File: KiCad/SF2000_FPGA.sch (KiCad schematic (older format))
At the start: 15 parts, among them J10 Conn_02x01, J3 Conn_02x03_Odd_Even, J4 Conn_02x01, J8 Conn_02x01, J9 Conn_02x01, U18 74LVC2G14, U7 10M04SCE144

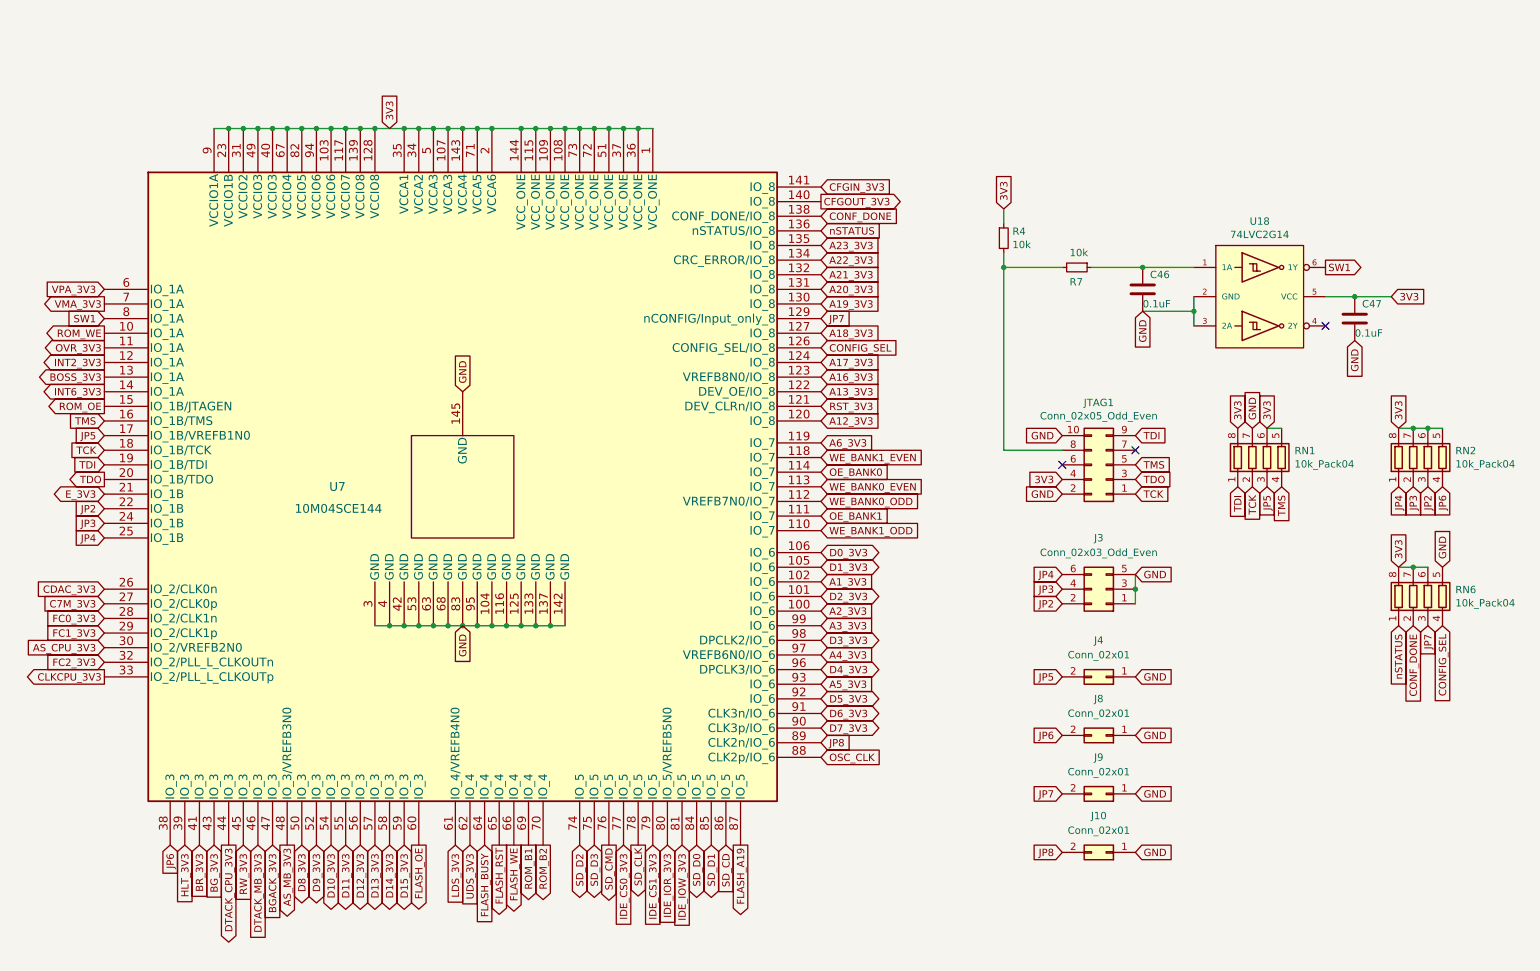
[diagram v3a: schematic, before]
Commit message: added IDE Activity LED-header and a header for IDE-pin 39 /Active
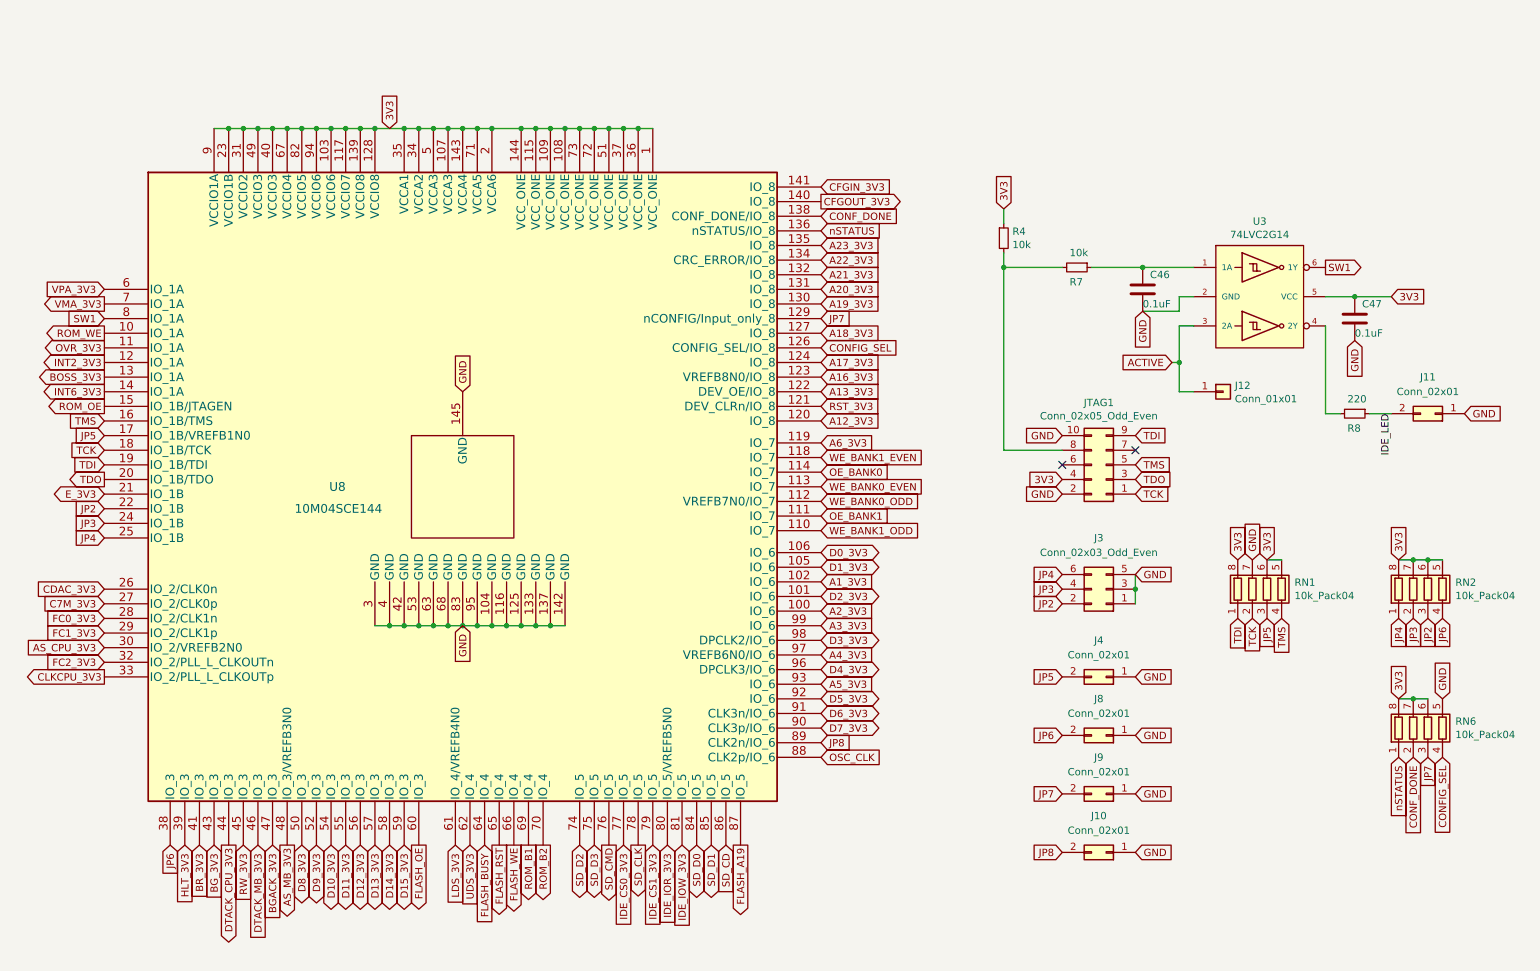
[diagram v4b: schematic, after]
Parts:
- added J11: Conn_02x01, Connector_PinHeader_2.54mm:PinHeader_2x01_P2.54mm_Vertical, symbol Connector_Generic:Conn_02x01
- added J12: Conn_01x01, Connector_PinHeader_2.54mm:PinHeader_1x01_P2.54mm_Vertical, symbol Connector_Generic:Conn_01x01
- added R8: 220, Resistor_SMD:R_0805_2012Metric_Pad1.15x1.40mm_HandSolder, symbol Device:R_Small
- renumbered U18 to U3
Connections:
- net GND: now also J11.1 (Pin_1); no longer U3.3 (2A)
- net at U3.4 (2Y): now also R8.2
- new net ACTIVE: J12.1 (Pin_1), U3.3 (2A)
- new net IDE_LED: J11.2 (Pin_2), R8.1
- no-connect marks 3 -> 2
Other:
- moved on the sheet: RN1, RN2, RN6
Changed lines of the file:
@@
 P 3800 3550
 AR Path="/62146C83" Ref="U7"  Part="1"
-AR Path="/620D263D/62146C83" Ref="U7"  Part="1"
-F 0 "U7" H 3000 3550 60  0000 R CNN
+AR Path="/620D263D/62146C83" Ref="U8"  Part="1"
+F 0 "U8" H 3000 3550 60  0000 R CNN
 F 1 "10M04SCE144" H 3250 3400 60  0000 R CNN
 F 2 "SF2000:EQFP-144-1EP_20x20mm_P0.5mm_EP5x5mm_TH_GND_pad" H 3800 3900 60  0001 C CNN
@@
 L Device:R_Pack04 RN1
 U 1 1 625F56E7
-P 9300 3350
-F 0 "RN1" H 9488 3396 50  0000 L CNN
-F 1 "10k_Pack04" H 9488 3305 50  0000 L CNN
-F 2 "SF2000:RESCAF80P320X160X60-8N" V 9575 3350 50  0001 C CNN
-F 3 "~" H 9300 3350 50  0001 C CNN
-	1    9300 3350
-	1    0    0    -1
-$EndComp
-Text GLabel 9100 3150 1    50   Input ~ 0
-3V3
-Text GLabel 9100 3550 3    50   Input ~ 0
+P 9300 4250
+F 0 "RN1" H 9488 4296 50  0000 L CNN
+F 1 "10k_Pack04" H 9488 4205 50  0000 L CNN
+F 2 "SF2000:RESCAF80P320X160X60-8N" V 9575 4250 50  0001 C CNN
+F 3 "~" H 9300 4250 50  0001 C CNN
+	1    9300 4250
+	1    0    0    -1
+$EndComp
+Text GLabel 9100 4050 1    50   Input ~ 0
+3V3
+Text GLabel 9100 4450 3    50   Input ~ 0
 TDI
-Text GLabel 9200 3550 3    50   Input ~ 0
+Text GLabel 9200 4450 3    50   Input ~ 0
 TCK
-Text GLabel 9400 3550 3    50   Input ~ 0
+Text GLabel 9400 4450 3    50   Input ~ 0
 TMS
-Text GLabel 9300 3550 3    50   Input ~ 0
+Text GLabel 9300 4450 3    50   Input ~ 0
 JP5
-Text GLabel 9200 3150 1    50   Input ~ 0
+Text GLabel 9200 4050 1    50   Input ~ 0
 GND
 Text GLabel 1350 3700 0    50   Input ~ 0
 JP2
-Text GLabel 9300 3150 1    50   Input ~ 0
-3V3
-Wire Wire Line
-	9300 3150 9400 3150
+Text GLabel 9300 4050 1    50   Input ~ 0
+3V3
+Wire Wire Line
+	9300 4050 9400 4050
 $Comp
 L Device:R_Pack04 RN2
 U 1 1 6265DCDE
-P 10400 3350
-F 0 "RN2" H 10588 3396 50  0000 L CNN
-F 1 "10k_Pack04" H 10588 3305 50  0000 L CNN
-F 2 "SF2000:RESCAF80P320X160X60-8N" V 10675 3350 50  0001 C CNN
-F 3 "~" H 10400 3350 50  0001 C CNN
-	1    10400 3350
-	1    0    0    -1
-$EndComp
-Text GLabel 10200 3150 1    50   Input ~ 0
-3V3
-Wire Wire Line
-	10200 3150 10300 3150
-Connection ~ 10300 3150
-Wire Wire Line
-	10300 3150 10400 3150
-Connection ~ 10400 3150
-Wire Wire Line
-	10400 3150 10500 3150
-Text GLabel 10200 4500 3    50   Input ~ 0
+P 10400 4250
+F 0 "RN2" H 10588 4296 50  0000 L CNN
+F 1 "10k_Pack04" H 10588 4205 50  0000 L CNN
+F 2 "SF2000:RESCAF80P320X160X60-8N" V 10675 4250 50  0001 C CNN
+F 3 "~" H 10400 4250 50  0001 C CNN
+	1    10400 4250
+	1    0    0    -1
+$EndComp
+Text GLabel 10200 4050 1    50   Input ~ 0
+3V3
+Wire Wire Line
+	10200 4050 10300 4050
+Connection ~ 10300 4050
+Wire Wire Line
+	10300 4050 10400 4050
+Connection ~ 10400 4050
+Wire Wire Line
+	10400 4050 10500 4050
+Text GLabel 10200 5400 3    50   Input ~ 0
 nSTATUS
-Text GLabel 10300 4500 3    50   Input ~ 0
+Text GLabel 10300 5400 3    50   Input ~ 0
 CONF_DONE
-Text GLabel 10200 3550 3    50   Input ~ 0
+Text GLabel 10200 4450 3    50   Input ~ 0
 JP4
-Text GLabel 10300 3550 3    50   Input ~ 0
+Text GLabel 10300 4450 3    50   Input ~ 0
 JP3
 Text GLabel 7500 1650 1    50   Input ~ 0
@@
 Text GLabel 1350 3200 0    50   Input ~ 0
 JP5
-Text GLabel 10400 3550 3    50   Input ~ 0
+Text GLabel 10400 4450 3    50   Input ~ 0
 JP2
 Text GLabel 1350 2300 0    50   Output ~ 0
@@
 L Device:R_Pack04 RN6
 U 1 1 62107318
-P 10400 4300
-F 0 "RN6" H 10588 4346 50  0000 L CNN
-F 1 "10k_Pack04" H 10588 4255 50  0000 L CNN
-F 2 "SF2000:RESCAF80P320X160X60-8N" V 10675 4300 50  0001 C CNN
-F 3 "~" H 10400 4300 50  0001 C CNN
-	1    10400 4300
-	1    0    0    -1
-$EndComp
-Text GLabel 10500 4500 3    50   Input ~ 0
+P 10400 5200
+F 0 "RN6" H 10588 5246 50  0000 L CNN
+F 1 "10k_Pack04" H 10588 5155 50  0000 L CNN
+F 2 "SF2000:RESCAF80P320X160X60-8N" V 10675 5200 50  0001 C CNN
+F 3 "~" H 10400 5200 50  0001 C CNN
+	1    10400 5200
+	1    0    0    -1
+$EndComp
+Text GLabel 10500 5400 3    50   Input ~ 0
 CONFIG_SEL
-Text GLabel 10200 4100 1    50   Input ~ 0
-3V3
-Wire Wire Line
-	10200 4100 10300 4100
-Text GLabel 10500 4100 1    50   Input ~ 0
+Text GLabel 10200 5000 1    50   Input ~ 0
+3V3
+Wire Wire Line
+	10200 5000 10300 5000
+Text GLabel 10500 5000 1    50   Input ~ 0
 GND
 Text GLabel 6250 2400 2    50   Input ~ 0
@@
 ROM_B2
 Wire Wire Line
-	10300 4100 10400 4100
-Connection ~ 10300 4100
-Text GLabel 10400 4500 3    50   Input ~ 0
+	10300 5000 10400 5000
+Connection ~ 10300 5000
+Text GLabel 10400 5400 3    50   Input ~ 0
 JP7
 Text GLabel 7900 5250 0    50   Input ~ 0
@@
 Text GLabel 8400 5250 2    50   Input ~ 0
 GND
-Text GLabel 10500 3550 3    50   Input ~ 0
+Text GLabel 10500 4450 3    50   Input ~ 0
 JP6
 Text GLabel 1800 6000 3    50   Input ~ 0
 JP6
 $Comp
-L SF2000:74LVC2G14 U18
+L SF2000:74LVC2G14 U3
 U 1 1 623FD973
 P 9250 2250
-F 0 "U18" H 9250 2765 50  0000 C CNN
+F 0 "U3" H 9250 2765 50  0000 C CNN
 F 1 "74LVC2G14" H 9250 2674 50  0000 C CNN
 F 2 "Package_SO:TSOP-6_1.65x3.05mm_P0.95mm" H 9750 3200 50  0001 C CNN
@@
 	1    0    0    -1
 $EndComp
-NoConn ~ 9700 2450
 Text GLabel 8450 2350 3    50   Input ~ 0
 GND
-Wire Wire Line
-	8800 2250 8800 2350
 Text GLabel 10150 2250 2    50   Input ~ 0
 3V3
 Wire Wire Line
 	8450 2050 8800 2050
-Wire Wire Line
-	8450 2350 8800 2350
-Connection ~ 8800 2350
-Wire Wire Line
-	8800 2350 8800 2450
 $Comp
 L Device:C C?
@@
 	8100 2050 8450 2050
 Connection ~ 8450 2050
+Wire Wire Line
+	8450 2350 8700 2350
+Wire Wire Line
+	8700 2350 8700 2250
+Wire Wire Line
+	8700 2250 8800 2250
+Text GLabel 8650 2700 0    50   Input ~ 0
+ACTIVE
+Wire Wire Line
+	8800 2450 8700 2450
+Wire Wire Line
+	8700 2450 8700 2700
+Wire Wire Line
+	8700 2700 8650 2700
+$Comp
+L Device:R_Small R?
+U 1 1 625C5BBC
+P 9900 3050
+AR Path="/625C5BBC" Ref="R?"  Part="1"
+AR Path="/620D263D/625C5BBC" Ref="R8"  Part="1"
+F 0 "R8" V 10000 3000 50  0000 L CNN
+F 1 "220" V 9800 3000 50  0000 L CNN
+F 2 "Resistor_SMD:R_0805_2012Metric_Pad1.15x1.40mm_HandSolder" H 9900 3050 50  0001 C CNN
+F 3 "~" H 9900 3050 50  0001 C CNN
+	1    9900 3050
+	0    1    1    0
+$EndComp
+Wire Wire Line
+	9700 2450 9700 3050
+Wire Wire Line
+	9700 3050 9800 3050
+$Comp
+L Connector_Generic:Conn_02x01 J11
+U 1 1 625CA23F
+P 10450 3050
+F 0 "J11" H 10500 2800 50  0000 C CNN
+F 1 "Conn_02x01" H 10500 2900 50  0000 C CNN
+F 2 "Connector_PinHeader_2.54mm:PinHeader_2x01_P2.54mm_Vertical" H 10450 3050 50  0001 C CNN
+F 3 "~" H 10450 3050 50  0001 C CNN
+	1    10450 3050
+	-1   0    0    1
+$EndComp
+Wire Wire Line
+	10000 3050 10150 3050
+Text GLabel 10650 3050 2    50   Input ~ 0
+GND
+Text Label 10150 3050 3    50   ~ 0
+IDE_LED
+$Comp
+L Connector_Generic:Conn_01x01 J12
+U 1 1 62602244
+P 9000 2900
+F 0 "J12" H 9080 2942 50  0000 L CNN
+F 1 "Conn_01x01" H 9080 2851 50  0000 L CNN
+F 2 "Connector_PinHeader_2.54mm:PinHeader_1x01_P2.54mm_Vertical" H 9000 2900 50  0001 C CNN
+F 3 "~" H 9000 2900 50  0001 C CNN
+	1    9000 2900
+	1    0    0    -1
+$EndComp
+Wire Wire Line
+	8700 2700 8700 2900
+Wire Wire Line
+	8700 2900 8800 2900
+Connection ~ 8700 2700
 $EndSCHEMATC

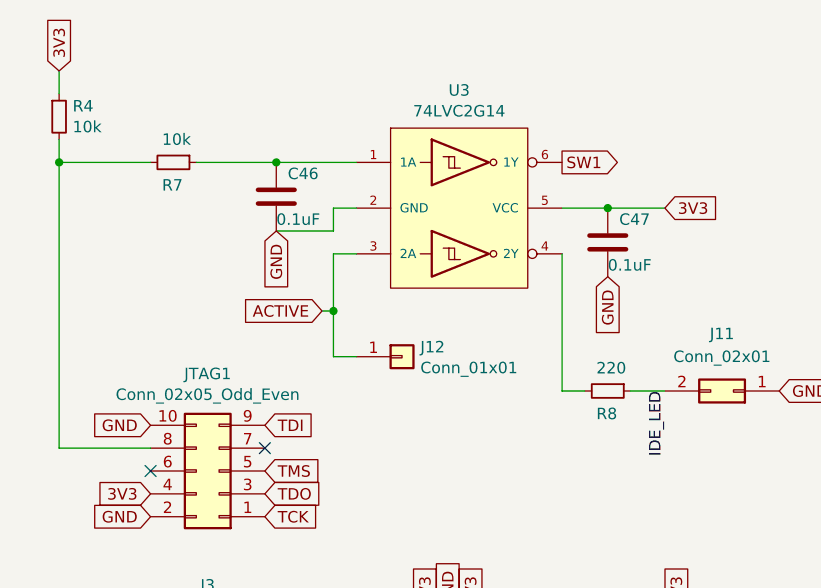
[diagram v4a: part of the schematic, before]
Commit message: fixed labeling/enumeration of caps and resistors, and some silkscreen fixes
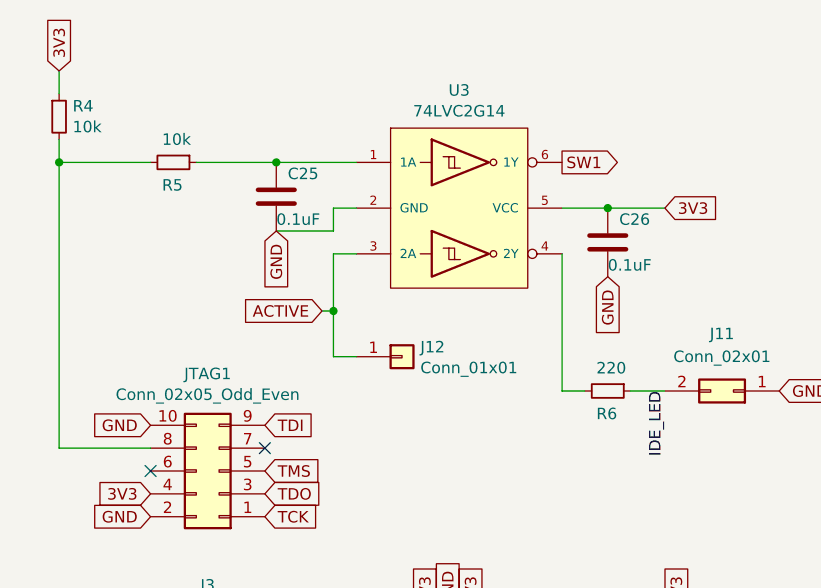
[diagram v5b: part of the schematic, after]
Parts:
- renumbered C46 to C25, C47 to C26, R7 to R5, R8 to R6
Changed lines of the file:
@@
 P 8450 2200
 AR Path="/624A6DA8" Ref="C?"  Part="1"
-AR Path="/620D263D/624A6DA8" Ref="C46"  Part="1"
-F 0 "C46" H 8500 2300 50  0000 L CNN
+AR Path="/620D263D/624A6DA8" Ref="C25"  Part="1"
+F 0 "C25" H 8500 2300 50  0000 L CNN
 F 1 "0.1uF" H 8450 2100 50  0000 L CNN
 F 2 "Capacitor_SMD:C_0805_2012Metric_Pad1.15x1.40mm_HandSolder" H 8488 2050 50  0001 C CNN
@@
 P 9900 2400
 AR Path="/624B4CFC" Ref="C?"  Part="1"
-AR Path="/620D263D/624B4CFC" Ref="C47"  Part="1"
-F 0 "C47" H 9950 2500 50  0000 L CNN
+AR Path="/620D263D/624B4CFC" Ref="C26"  Part="1"
+F 0 "C26" H 9950 2500 50  0000 L CNN
 F 1 "0.1uF" H 9900 2300 50  0000 L CNN
 F 2 "Capacitor_SMD:C_0805_2012Metric_Pad1.15x1.40mm_HandSolder" H 9938 2250 50  0001 C CNN
@@
 P 8000 2050
 AR Path="/62519236" Ref="R?"  Part="1"
-AR Path="/620D263D/62519236" Ref="R7"  Part="1"
-F 0 "R7" V 8100 2000 50  0000 L CNN
+AR Path="/620D263D/62519236" Ref="R5"  Part="1"
+F 0 "R5" V 8100 2000 50  0000 L CNN
 F 1 "10k" V 7900 2000 50  0000 L CNN
 F 2 "Resistor_SMD:R_0805_2012Metric_Pad1.15x1.40mm_HandSolder" H 8000 2050 50  0001 C CNN
@@
 P 9900 3050
 AR Path="/625C5BBC" Ref="R?"  Part="1"
-AR Path="/620D263D/625C5BBC" Ref="R8"  Part="1"
-F 0 "R8" V 10000 3000 50  0000 L CNN
+AR Path="/620D263D/625C5BBC" Ref="R6"  Part="1"
+F 0 "R6" V 10000 3000 50  0000 L CNN
 F 1 "220" V 9800 3000 50  0000 L CNN
 F 2 "Resistor_SMD:R_0805_2012Metric_Pad1.15x1.40mm_HandSolder" H 9900 3050 50  0001 C CNN
